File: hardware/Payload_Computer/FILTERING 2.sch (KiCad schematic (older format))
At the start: 3 parts

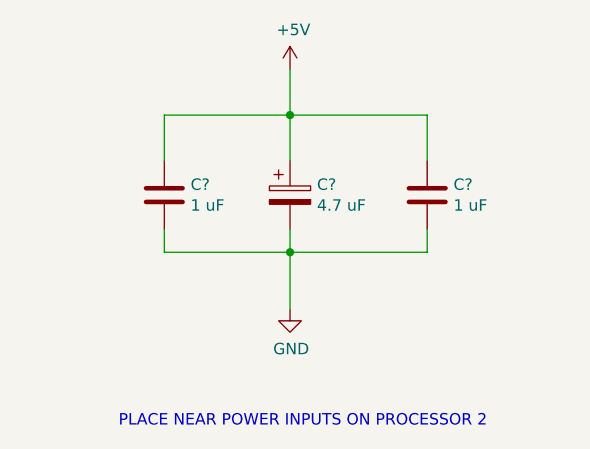
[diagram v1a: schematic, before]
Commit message: Finished BNO055
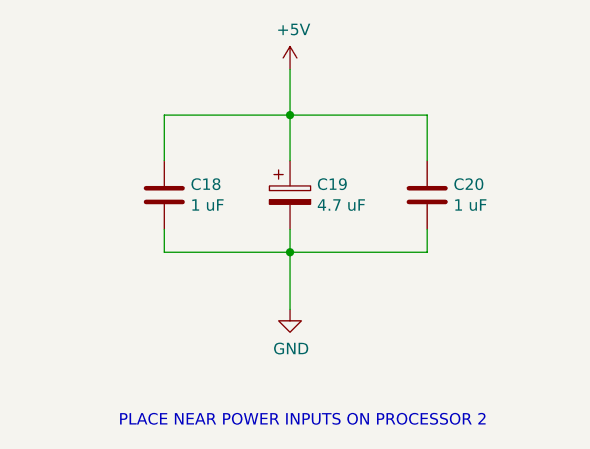
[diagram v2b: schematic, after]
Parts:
- gave numbers to parts that had none: 3
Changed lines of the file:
@@
 $Descr A4 11693 8268
 encoding utf-8
-Sheet 13 17
+Sheet 13 15
 Title ""
 Date ""
@@
 $EndDescr
 $Comp
-L Device:C C?
+L Device:C C18
 U 1 1 5F9988E5
 P 5200 3750
-F 0 "C?" H 5315 3796 50  0000 L CNN
+F 0 "C18" H 5315 3796 50  0000 L CNN
 F 1 "1 uF" H 5315 3705 50  0000 L CNN
 F 2 "" H 5238 3600 50  0001 C CNN
@@
 $EndComp
 $Comp
-L Device:C C?
+L Device:C C20
 U 1 1 5F9988EB
 P 6350 3750
-F 0 "C?" H 6465 3796 50  0000 L CNN
+F 0 "C20" H 6465 3796 50  0000 L CNN
 F 1 "1 uF" H 6465 3705 50  0000 L CNN
 F 2 "" H 6388 3600 50  0001 C CNN
@@
 $EndComp
 $Comp
-L Device:CP C?
+L Device:CP C19
 U 1 1 5F9988F1
 P 5750 3750
-F 0 "C?" H 5868 3796 50  0000 L CNN
+F 0 "C19" H 5868 3796 50  0000 L CNN
 F 1 "4.7 uF" H 5868 3705 50  0000 L CNN
 F 2 "" H 5788 3600 50  0001 C CNN
@@
 $EndComp
 $Comp
-L power:+5V #PWR?
+L power:+5V #PWR0141
 U 1 1 5F9988F7
 P 5750 3200
-F 0 "#PWR?" H 5750 3050 50  0001 C CNN
+F 0 "#PWR0141" H 5750 3050 50  0001 C CNN
 F 1 "+5V" H 5765 3373 50  0000 C CNN
 F 2 "" H 5750 3200 50  0001 C CNN
@@
 $EndComp
 $Comp
-L power:GND #PWR?
+L power:GND #PWR0142
 U 1 1 5F9988FD
 P 5750 4250
-F 0 "#PWR?" H 5750 4000 50  0001 C CNN
+F 0 "#PWR0142" H 5750 4000 50  0001 C CNN
 F 1 "GND" H 5755 4077 50  0000 C CNN
 F 2 "" H 5750 4250 50  0001 C CNN

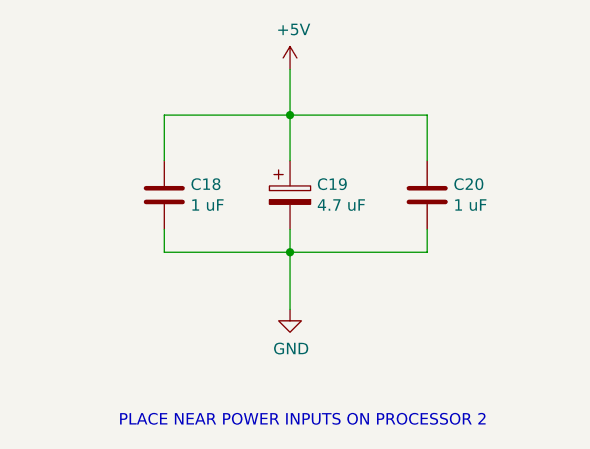
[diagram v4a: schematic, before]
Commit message: Added a power regulation sheet. Added indication LED for Teensy. Fixed Teensy filtering
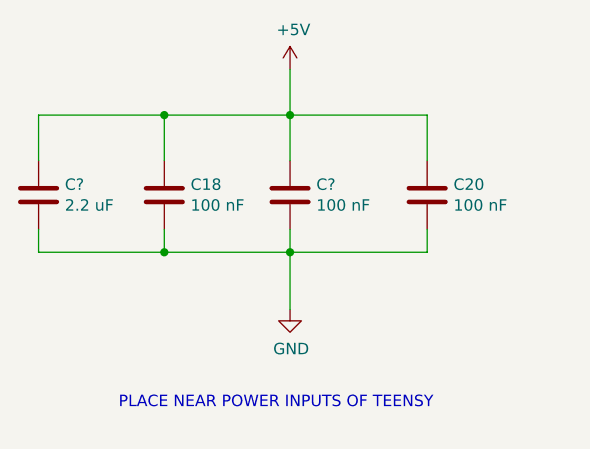
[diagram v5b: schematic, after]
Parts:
- removed C19: 4.7 uF, symbol Device:CP
- added C?: 100 nF, symbol Device:C
- added C?: 2.2 uF, symbol Device:C
- C18, C20: value 1 uF -> 100 nF
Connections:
- net +5V: now also C?.1, C?.1
- net GND: now also C?.2, C?.2
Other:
- note added: "PLACE NEAR POWER INPUTS OF TEENSY \n\n\n"
- note removed: "PLACE NEAR POWER INPUTS ON PROCESSOR 2\n\n"
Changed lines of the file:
@@
 $Descr A4 11693 8268
 encoding utf-8
-Sheet 13 13
+Sheet 10 14
 Title ""
 Date ""
@@
 P 5200 3750
 F 0 "C18" H 5315 3796 50  0000 L CNN
-F 1 "1 uF" H 5315 3705 50  0000 L CNN
+F 1 "100 nF" H 5315 3705 50  0000 L CNN
 F 2 "" H 5238 3600 50  0001 C CNN
 F 3 "~" H 5200 3750 50  0001 C CNN
@@
 P 6350 3750
 F 0 "C20" H 6465 3796 50  0000 L CNN
-F 1 "1 uF" H 6465 3705 50  0000 L CNN
+F 1 "100 nF" H 6465 3705 50  0000 L CNN
 F 2 "" H 6388 3600 50  0001 C CNN
 F 3 "~" H 6350 3750 50  0001 C CNN
 	1    6350 3750
-	1    0    0    -1
-$EndComp
-$Comp
-L Device:CP C19
-U 1 1 5F9988F1
-P 5750 3750
-F 0 "C19" H 5868 3796 50  0000 L CNN
-F 1 "4.7 uF" H 5868 3705 50  0000 L CNN
-F 2 "" H 5788 3600 50  0001 C CNN
-F 3 "~" H 5750 3750 50  0001 C CNN
-	1    5750 3750
 	1    0    0    -1
 $EndComp
@@
 	6350 3400 5750 3400
 Text Notes 5000 4850 0    50   ~ 0
-PLACE NEAR POWER INPUTS ON PROCESSOR 2\n\n
+PLACE NEAR POWER INPUTS OF TEENSY \n\n\n
+$Comp
+L Device:C C?
+U 1 1 5FC1F499
+P 5750 3750
+F 0 "C?" H 5865 3796 50  0000 L CNN
+F 1 "100 nF" H 5865 3705 50  0000 L CNN
+F 2 "" H 5788 3600 50  0001 C CNN
+F 3 "~" H 5750 3750 50  0001 C CNN
+	1    5750 3750
+	1    0    0    -1
+$EndComp
+$Comp
+L Device:C C?
+U 1 1 5FC1F8C7
+P 4650 3750
+F 0 "C?" H 4765 3796 50  0000 L CNN
+F 1 "2.2 uF" H 4765 3705 50  0000 L CNN
+F 2 "" H 4688 3600 50  0001 C CNN
+F 3 "~" H 4650 3750 50  0001 C CNN
+	1    4650 3750
+	1    0    0    -1
+$EndComp
+Wire Wire Line
+	5200 3400 4650 3400
+Wire Wire Line
+	4650 3400 4650 3600
+Connection ~ 5200 3400
+Wire Wire Line
+	4650 3900 4650 4000
+Wire Wire Line
+	4650 4000 5200 4000
+Connection ~ 5200 4000
 $EndSCHEMATC
